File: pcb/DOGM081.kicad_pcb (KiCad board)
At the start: 2 copper layers, 51.8 x 31.5 mm, 8 parts, among them P1 CONN_01X06, U1 EA_DOGMxxx-A

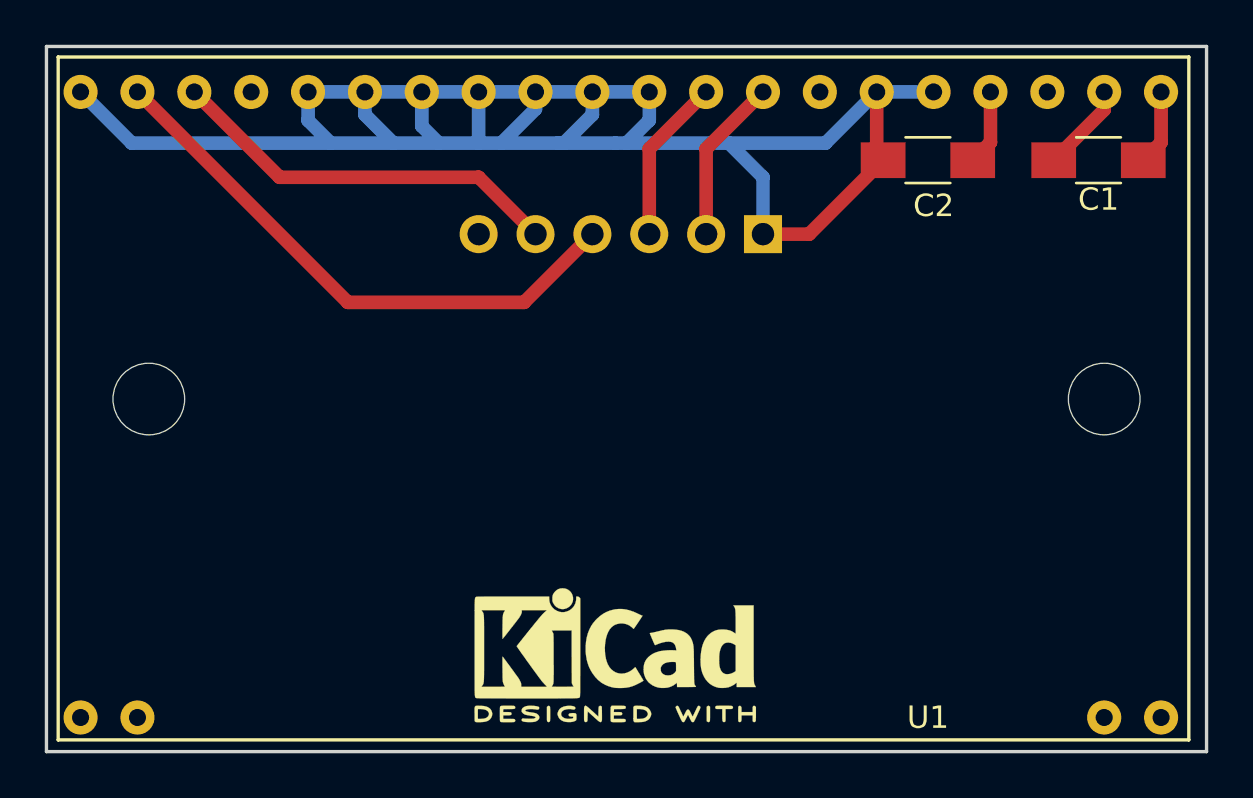
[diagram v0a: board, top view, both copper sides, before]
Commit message: Complted the Rev2 layout and sent to OSHPark. Feature for back-light
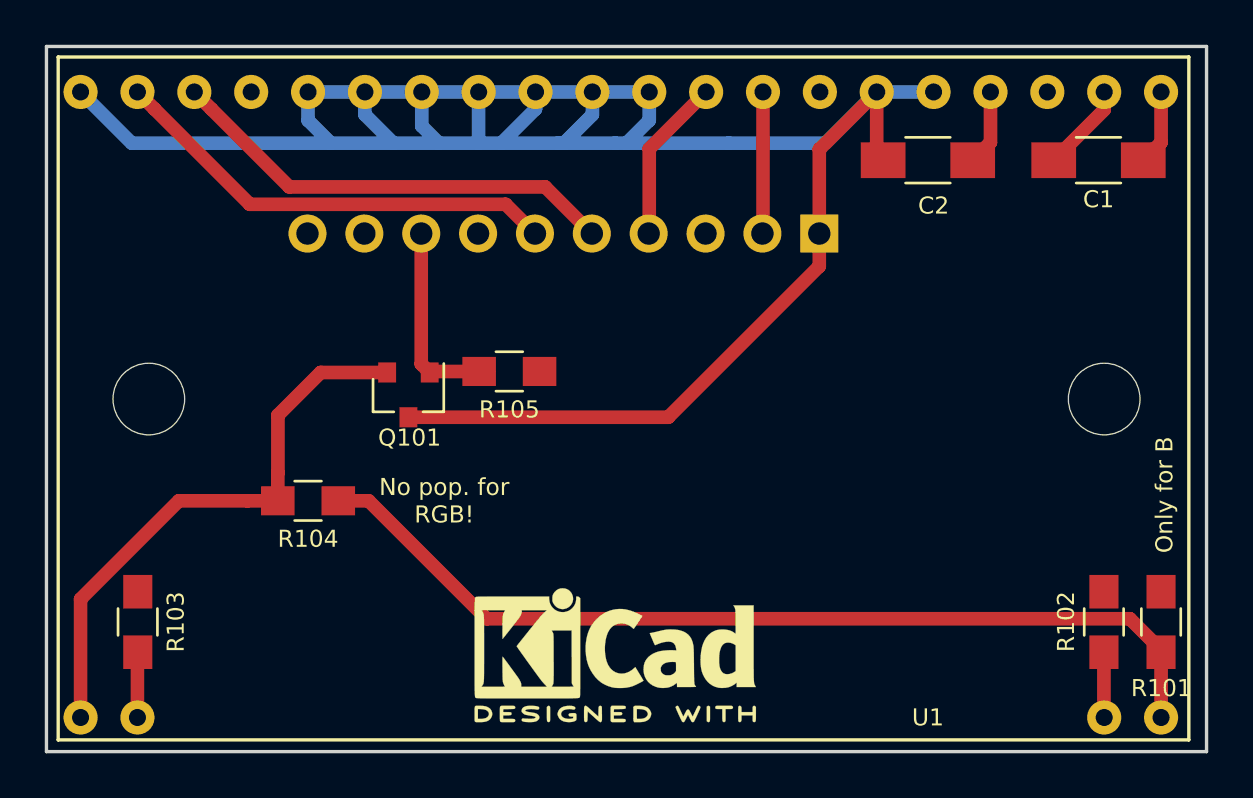
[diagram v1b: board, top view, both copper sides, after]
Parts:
- removed P1: CONN_01X06, Socket_Strips:Socket_Strip_Straight_1x06_Pitch2.54mm
- added J101: Conn_01x10_Male, Pin_Headers:Pin_Header_Straight_1x10_Pitch2.54mm, B.Cu at (182.9, 78.5)
- added Q101: IRLML2502GTRPBF, TO_SOT_Packages_SMD:SOT-23, F.Cu at (164.5, 85.7)
- added R101: R, Resistors_SMD:R_0805_HandSoldering, F.Cu at (198.1, 95.8)
- added R102: R, Resistors_SMD:R_0805_HandSoldering, F.Cu at (195.6, 95.8)
- added R103: R, Resistors_SMD:R_0805_HandSoldering, F.Cu at (152.4, 95.8)
- added R104: R, Resistors_SMD:R_0805_HandSoldering, F.Cu at (160.0, 90.4)
- added R105: R, Resistors_SMD:R_0805_HandSoldering, F.Cu at (169.0, 84.6)
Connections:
- U1 pad 1: (no net) -> /A1_A
- U1 pad 19: (no net) -> /C2_G
- U1 pad 2: (no net) -> /C1_R
- U1 pad 20: (no net) -> /A2_B
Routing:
- net /A2_B: track 0.00 -> 42.7 mm
- net /A1_A: track 0.00 -> 25.4 mm
- net /Vdd: track 88.9 -> 107.5 mm
- net /BACKLIGHT: track 0.00 -> 9.17 mm
- net /RS: track 25.5 -> 20.4 mm
- net /C2_G: track 0.00 -> 2.92 mm
- net /C1_R: track 0.00 -> 2.92 mm
- net /CSB: track 17.9 -> 20.4 mm
- net /MOSI: track 7.40 -> 6.34 mm
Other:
- board text added: "BK_LT"
- board text added: "CS"
- board text added: "DOGM081 Adapter 2L_2"
- board text added: "N/C"
- board text added: "No pop. for RGB!"
- board text added: "Only for B"
- board text removed: "CSB"
- board text removed: "DOGM081 Adapter 2L_1"
